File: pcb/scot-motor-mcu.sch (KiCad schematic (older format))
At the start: 49 parts, among them IC2 STM32F0xxKxTx, IC3 NCV8450A, J8 Conn_01x03_Male, P1 SWD, Q1 BC817, U1 LTV-357T, U10 74AHC1G08, U2 74HC00, U3 LTV-357T, U4 LTV-357T, U5 DRV8872DDA, Y1 Crystal_GND24

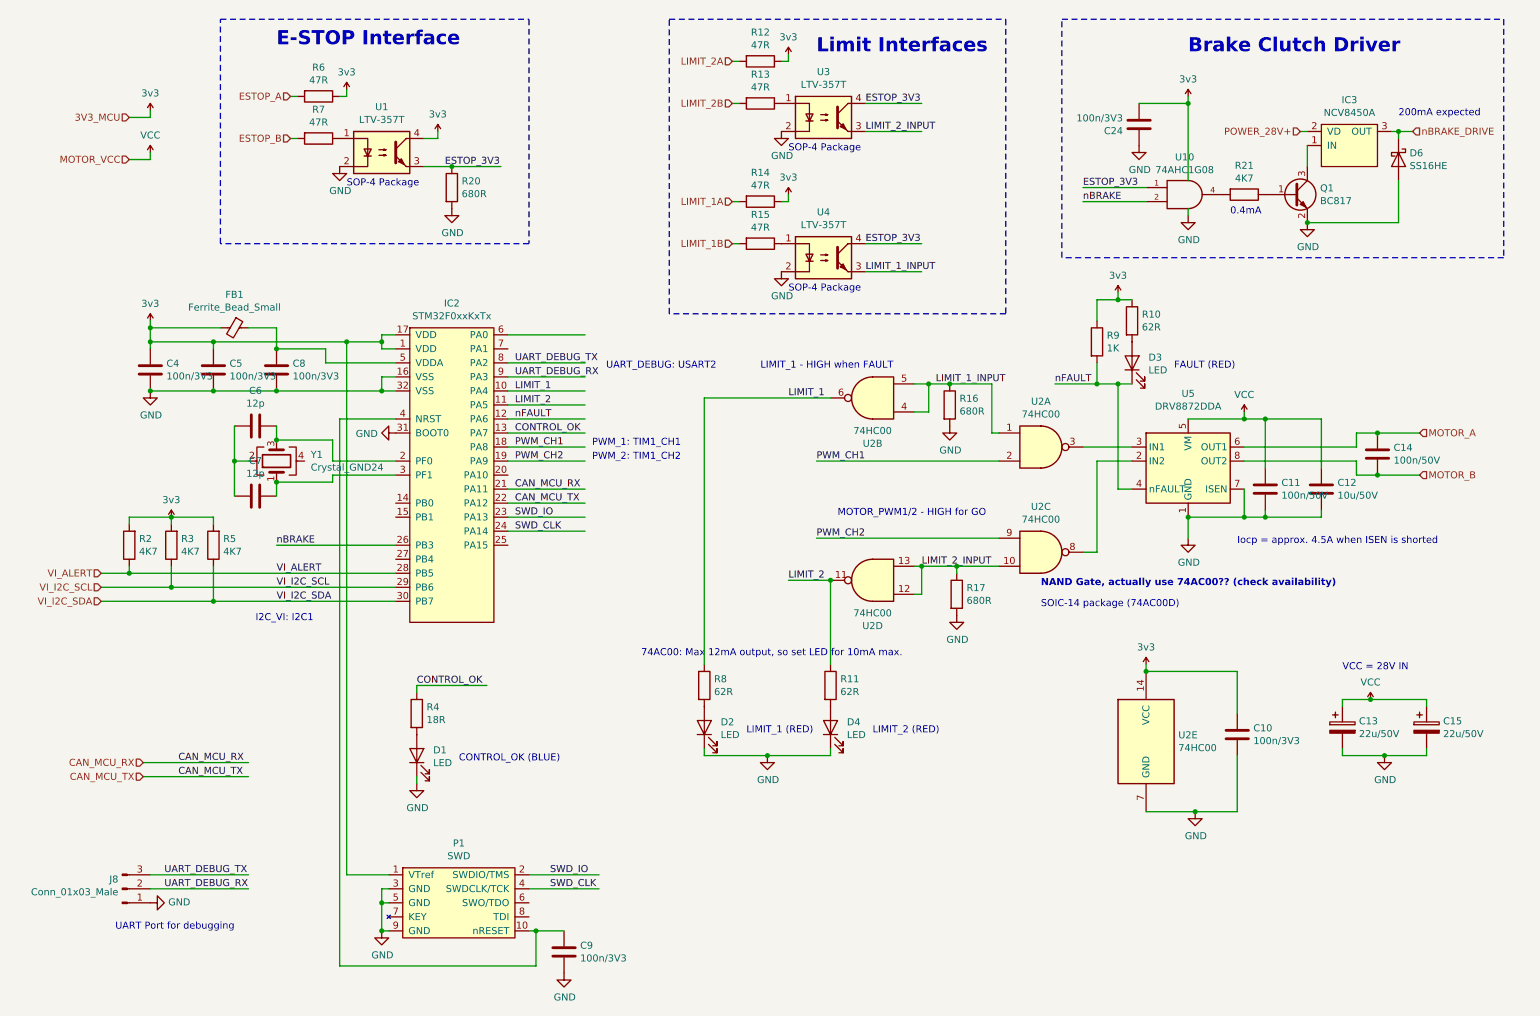
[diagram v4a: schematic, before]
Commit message: PCB progress, schematic fixes.
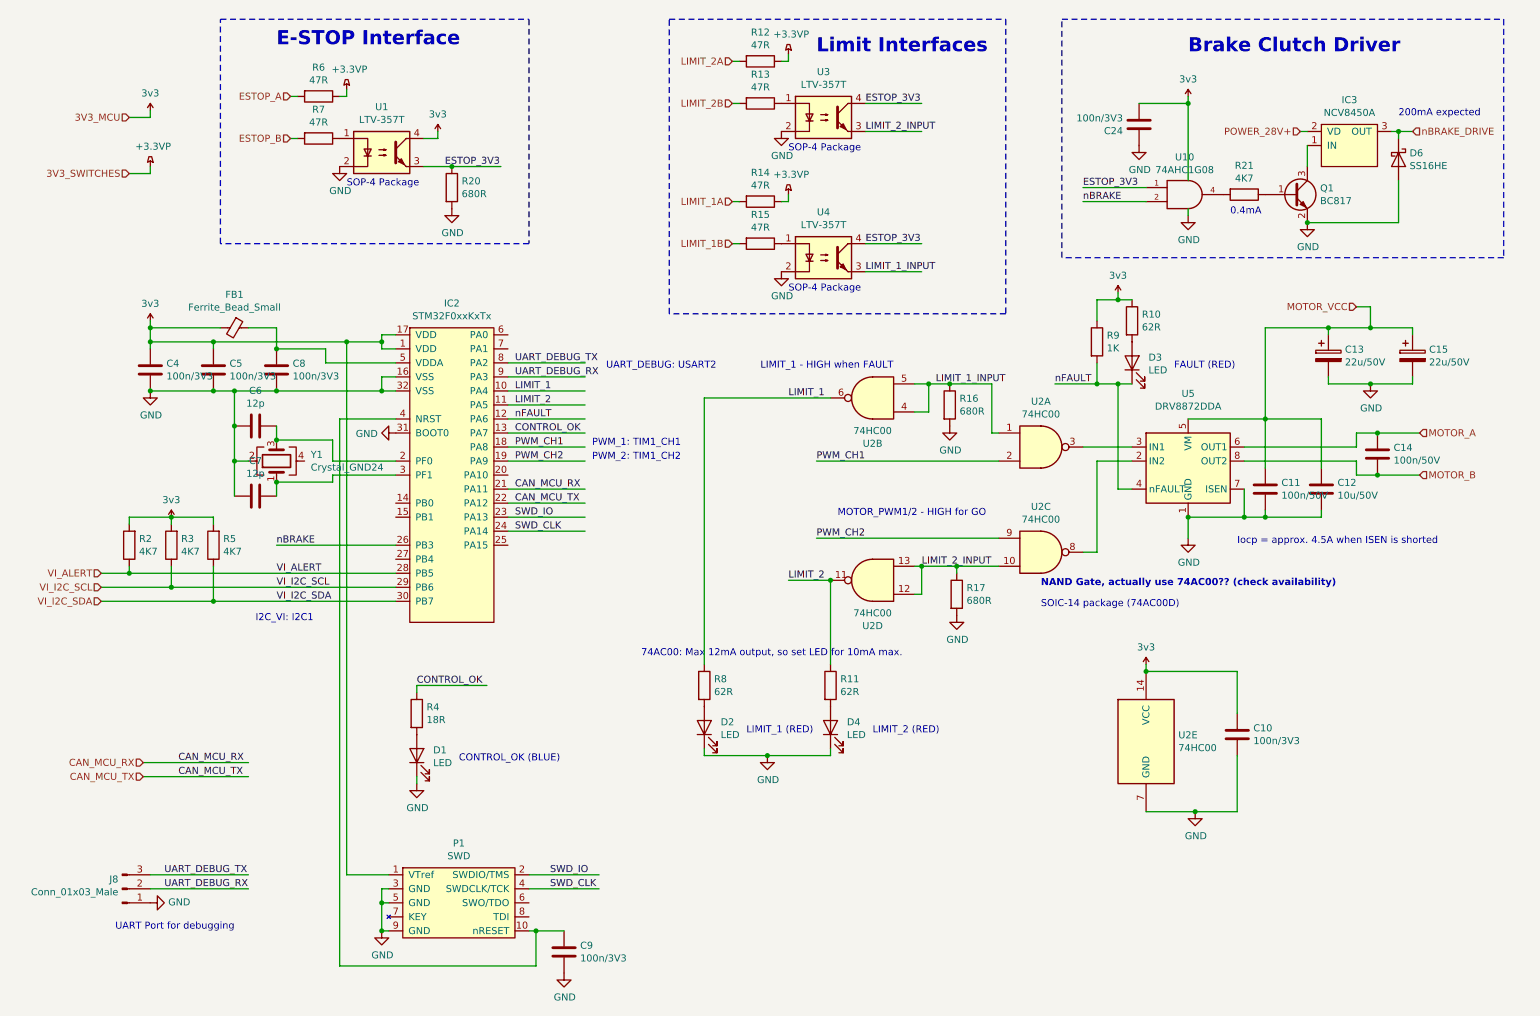
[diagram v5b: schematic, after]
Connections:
- net labels added: +3.3VP, 3V3_SWITCHES
- net labels removed: VCC
- wire segments 193 -> 196
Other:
- note removed: "VCC = 28V IN"
- moved on the sheet: C13, C15
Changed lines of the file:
@@
 	9450 3850 9450 3500
-Wire Wire Line
-	9450 3500 9300 3500
 Wire Wire Line
 	9450 3500 9850 3500
@@
 	9250 5300 8600 5300
 Connection ~ 8600 5300
-$Comp
-L agg-kicad:VCC #PWR0105
-U 1 1 5E6313B5
-P 9300 3450
-F 0 "#PWR0105" H 9300 3560 50  0001 L CNN
-F 1 "VCC" H 9300 3573 50  0000 C CNN
-F 2 "" H 9300 3450 50  0001 C CNN
-F 3 "" H 9300 3450 50  0001 C CNN
-	1    9300 3450
-	1    0    0    -1
-$EndComp
-Connection ~ 9300 3500
-Wire Wire Line
-	9300 3500 8900 3500
 Text HLabel 5650 950  0    50   Input ~ 0
 LIMIT_2A
@@
 Text Notes 6400 4200 0    50   ~ 0
 MOTOR_PWM1/2 - HIGH for GO
-Wire Wire Line
-	9300 3450 9300 3500
-$Comp
-L agg-kicad:VCC #PWR0106
-U 1 1 5E6A00FE
-P 10200 5500
-F 0 "#PWR0106" H 10200 5610 50  0001 L CNN
-F 1 "VCC" H 10200 5623 50  0000 C CNN
-F 2 "" H 10200 5500 50  0001 C CNN
-F 3 "" H 10200 5500 50  0001 C CNN
-	1    10200 5500
-	1    0    0    -1
-$EndComp
 $Comp
 L Device:CP C13
 U 1 1 5E6A417D
-P 10000 5700
-F 0 "C13" H 10118 5746 50  0000 L CNN
-F 1 "22u/50V" H 10118 5655 50  0000 L CNN
-F 2 "Capacitor_SMD:CP_Elec_8x10.5" H 10038 5550 50  0001 C CNN
-F 3 "~" H 10000 5700 50  0001 C CNN
-	1    10000 5700
+P 9900 3050
+F 0 "C13" H 10018 3096 50  0000 L CNN
+F 1 "22u/50V" H 10018 3005 50  0000 L CNN
+F 2 "Capacitor_SMD:CP_Elec_8x10.5" H 9938 2900 50  0001 C CNN
+F 3 "~" H 9900 3050 50  0001 C CNN
+	1    9900 3050
 	1    0    0    -1
 $EndComp
@@
 L Device:CP C15
 U 1 1 5E6A4BEF
-P 10600 5700
-F 0 "C15" H 10718 5746 50  0000 L CNN
-F 1 "22u/50V" H 10718 5655 50  0000 L CNN
-F 2 "Capacitor_SMD:CP_Elec_8x10.5" H 10638 5550 50  0001 C CNN
-F 3 "~" H 10600 5700 50  0001 C CNN
-	1    10600 5700
+P 10500 3050
+F 0 "C15" H 10618 3096 50  0000 L CNN
+F 1 "22u/50V" H 10618 3005 50  0000 L CNN
+F 2 "Capacitor_SMD:CP_Elec_8x10.5" H 10538 2900 50  0001 C CNN
+F 3 "~" H 10500 3050 50  0001 C CNN
+	1    10500 3050
 	1    0    0    -1
 $EndComp
 Text Notes 7850 4700 0    50   ~ 10
 NAND Gate, actually use 74AC00?? (check availability)
-Text Notes 10000 5300 0    50   ~ 0
-VCC = 28V IN
 $Comp
 L agg-kicad:STM32F0xxKxTx IC2
@@
 Text HLabel 2500 1200 0    50   Input ~ 0
 ESTOP_A
-$Comp
-L agg-kicad:3v3 #PWR0107
-U 1 1 5E8B86A8
-P 3550 1450
-F 0 "#PWR0107" H 3550 1560 50  0001 L CNN
-F 1 "3v3" H 3550 1573 50  0000 C CNN
-F 2 "" H 3550 1450 50  0001 C CNN
-F 3 "" H 3550 1450 50  0001 C CNN
-	1    3550 1450
-	1    0    0    -1
-$EndComp
 Wire Wire Line
 	8250 3800 8250 4450
@@
 Connection ~ 2400 3300
 Wire Wire Line
-	2400 3300 1950 3300
+	2400 3300 2100 3300
 Wire Wire Line
 	3250 3200 3150 3200
@@
 UART Port for debugging
 Wire Wire Line
-	10600 5900 10600 5850
-Wire Wire Line
-	10000 5900 10000 5850
-Wire Wire Line
-	10000 5550 10000 5500
-Wire Wire Line
-	10000 5500 10200 5500
-Wire Wire Line
-	10600 5550 10600 5500
-Wire Wire Line
-	10600 5500 10200 5500
-Connection ~ 10200 5500
+	10500 3250 10500 3200
+Wire Wire Line
+	9900 3250 9900 3200
+Wire Wire Line
+	9900 2900 9900 2850
+Wire Wire Line
+	10500 2900 10500 2850
 Wire Wire Line
 	6350 4650 6050 4650
@@
 $EndComp
 Wire Wire Line
-	10000 5900 10300 5900
+	9900 3250 10200 3250
 $Comp
 L power:GND #PWR0115
@@
 L power:GND #PWR0117
 U 1 1 5EB441CE
-P 10300 5900
-F 0 "#PWR0117" H 10300 5650 50  0001 C CNN
-F 1 "GND" H 10305 5727 50  0000 C CNN
-F 2 "" H 10300 5900 50  0001 C CNN
-F 3 "" H 10300 5900 50  0001 C CNN
-	1    10300 5900
-	1    0    0    -1
-$EndComp
-Connection ~ 10300 5900
-Wire Wire Line
-	10300 5900 10600 5900
+P 10200 3250
+F 0 "#PWR0117" H 10200 3000 50  0001 C CNN
+F 1 "GND" H 10205 3077 50  0000 C CNN
+F 2 "" H 10200 3250 50  0001 C CNN
+F 3 "" H 10200 3250 50  0001 C CNN
+	1    10200 3250
+	1    0    0    -1
+$EndComp
+Connection ~ 10200 3250
+Wire Wire Line
+	10200 3250 10500 3250
 Wire Wire Line
 	4050 4000 4600 4000
@@
 	1    0    0    -1
 $EndComp
-$Comp
-L agg-kicad:3v3 #PWR0119
-U 1 1 5EDDA568
-P 6050 900
-F 0 "#PWR0119" H 6050 1010 50  0001 L CNN
-F 1 "3v3" H 6050 1023 50  0000 C CNN
-F 2 "" H 6050 900 50  0001 C CNN
-F 3 "" H 6050 900 50  0001 C CNN
-	1    6050 900
-	1    0    0    -1
-$EndComp
 Wire Wire Line
 	6050 900  6050 950
@@
 L agg-kicad:3v3 #PWR0120
 U 1 1 5EF1DE63
-P 2900 1150
-F 0 "#PWR0120" H 2900 1260 50  0001 L CNN
-F 1 "3v3" H 2900 1273 50  0000 C CNN
-F 2 "" H 2900 1150 50  0001 C CNN
-F 3 "" H 2900 1150 50  0001 C CNN
-	1    2900 1150
+P 3550 1450
+F 0 "#PWR0120" H 3550 1560 50  0001 L CNN
+F 1 "3v3" H 3550 1573 50  0000 C CNN
+F 2 "" H 3550 1450 50  0001 C CNN
+F 3 "" H 3550 1450 50  0001 C CNN
+	1    3550 1450
 	1    0    0    -1
 $EndComp
@@
 	1    5850 2250
 	0    1    1    0
-$EndComp
-$Comp
-L agg-kicad:3v3 #PWR0121
-U 1 1 5EFDF057
-P 6050 1900
-F 0 "#PWR0121" H 6050 2010 50  0001 L CNN
-F 1 "3v3" H 6050 2023 50  0000 C CNN
-F 2 "" H 6050 1900 50  0001 C CNN
-F 3 "" H 6050 1900 50  0001 C CNN
-	1    6050 1900
-	1    0    0    -1
 $EndComp
 Wire Wire Line
@@
 	1950 4200 1950 4250
 Connection ~ 1650 4200
-$Comp
-L agg-kicad:VCC #PWR0124
-U 1 1 5F22A876
-P 1500 1600
-F 0 "#PWR0124" H 1500 1710 50  0001 L CNN
-F 1 "VCC" H 1500 1723 50  0000 C CNN
-F 2 "" H 1500 1600 50  0001 C CNN
-F 3 "" H 1500 1600 50  0001 C CNN
-	1    1500 1600
-	1    0    0    -1
-$EndComp
-Text HLabel 1350 1650 0    50   Input ~ 0
+Text HLabel 10100 2700 0    50   Input ~ 0
 MOTOR_VCC
-Wire Wire Line
-	1500 1600 1500 1650
-Wire Wire Line
-	1500 1650 1350 1650
 Text Notes 2250 4950 0    50   ~ 0
 I2C_VI: I2C1
@@
 Text Notes 9200 2050 0    50   ~ 0
 0.4mA
-Wire Wire Line
-	4050 2900 4600 2900
 Wire Wire Line
 	3250 4400 2400 4400
@@
 	7950 3250 8250 3250
 Connection ~ 8250 3250
+$Comp
+L power:+3.3VP #PWR0121
+U 1 1 5E945EEF
+P 1500 1700
+F 0 "#PWR0121" H 1650 1650 50  0001 C CNN
+F 1 "+3.3VP" H 1520 1843 50  0000 C CNN
+F 2 "" H 1500 1700 50  0001 C CNN
+F 3 "" H 1500 1700 50  0001 C CNN
+	1    1500 1700
+	1    0    0    -1
+$EndComp
+Text HLabel 1350 1750 0    50   Input ~ 0
+3V3_SWITCHES
+Wire Wire Line
+	1350 1750 1500 1750
+Wire Wire Line
+	1500 1750 1500 1700
+$Comp
+L power:+3.3VP #PWR0145
+U 1 1 5E962B75
+P 2900 1150
+F 0 "#PWR0145" H 3050 1100 50  0001 C CNN
+F 1 "+3.3VP" H 2920 1293 50  0000 C CNN
+F 2 "" H 2900 1150 50  0001 C CNN
+F 3 "" H 2900 1150 50  0001 C CNN
+	1    2900 1150
+	1    0    0    -1
+$EndComp
+$Comp
+L power:+3.3VP #PWR0146
+U 1 1 5E96A66C
+P 6050 900
+F 0 "#PWR0146" H 6200 850 50  0001 C CNN
+F 1 "+3.3VP" H 6070 1043 50  0000 C CNN
+F 2 "" H 6050 900 50  0001 C CNN
+F 3 "" H 6050 900 50  0001 C CNN
+	1    6050 900
+	1    0    0    -1
+$EndComp
+$Comp
+L power:+3.3VP #PWR0147
+U 1 1 5E96ADCE
+P 6050 1900
+F 0 "#PWR0147" H 6200 1850 50  0001 C CNN
+F 1 "+3.3VP" H 6070 2043 50  0000 C CNN
+F 2 "" H 6050 1900 50  0001 C CNN
+F 3 "" H 6050 1900 50  0001 C CNN
+	1    6050 1900
+	1    0    0    -1
+$EndComp
+Wire Wire Line
+	2100 3550 2100 3300
+Connection ~ 2100 3550
+Connection ~ 2100 3300
+Wire Wire Line
+	2100 3300 1950 3300
+Wire Wire Line
+	8900 3500 9450 3500
+Wire Wire Line
+	9900 2850 10200 2850
+Wire Wire Line
+	9450 3500 9450 2850
+Wire Wire Line
+	9450 2850 9900 2850
+Connection ~ 9900 2850
+Wire Wire Line
+	10200 2700 10200 2850
+Wire Wire Line
+	10100 2700 10200 2700
+Connection ~ 10200 2850
+Wire Wire Line
+	10200 2850 10500 2850
 $EndSCHEMATC

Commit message: PCB progress.
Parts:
- R21: value 4K7 -> 1K
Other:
- note removed: "0.4mA"
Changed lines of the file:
@@
 Wire Wire Line
 	9750 1550 9750 1700
-Text Notes 9200 2050 0    50   ~ 0
-0.4mA
 Wire Wire Line
 	3250 4400 2400 4400
@@
 P 9300 1900
 F 0 "R21" V 9093 1900 50  0000 C CNN
-F 1 "4K7" V 9184 1900 50  0000 C CNN
+F 1 "1K" V 9184 1900 50  0000 C CNN
 F 2 "Resistor_SMD:R_0603_1608Metric_Pad1.05x0.95mm_HandSolder" V 9230 1900 50  0001 C CNN
 F 3 "~" H 9300 1900 50  0001 C CNN

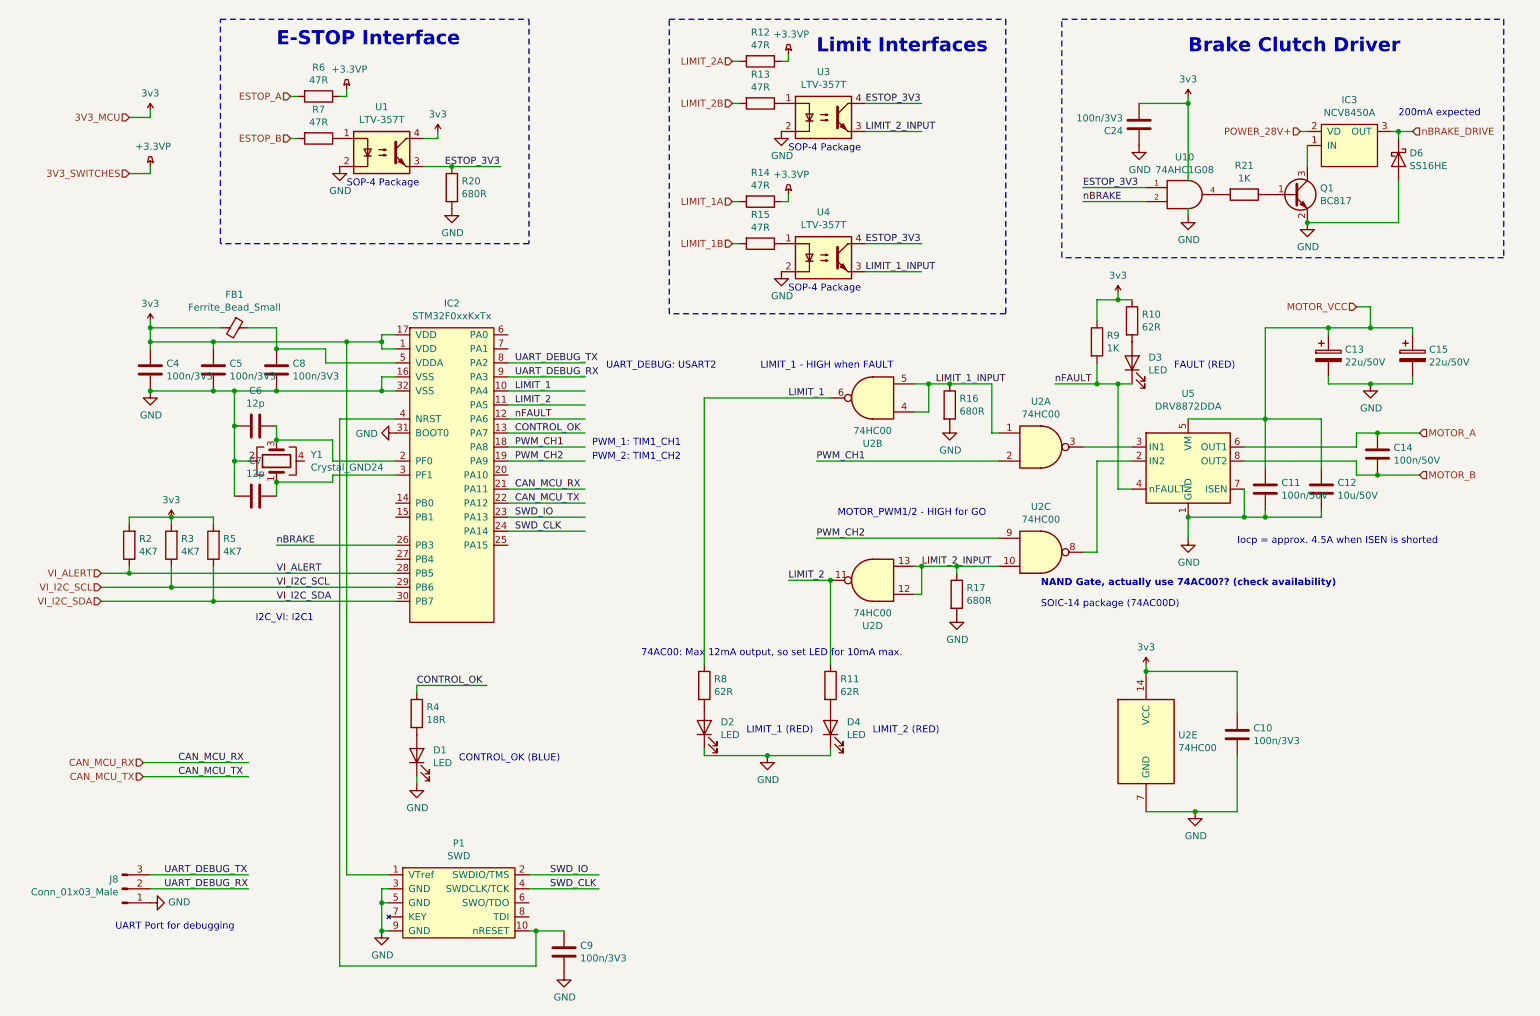
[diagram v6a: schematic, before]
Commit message: pcb: Add Clutch Release indicator.
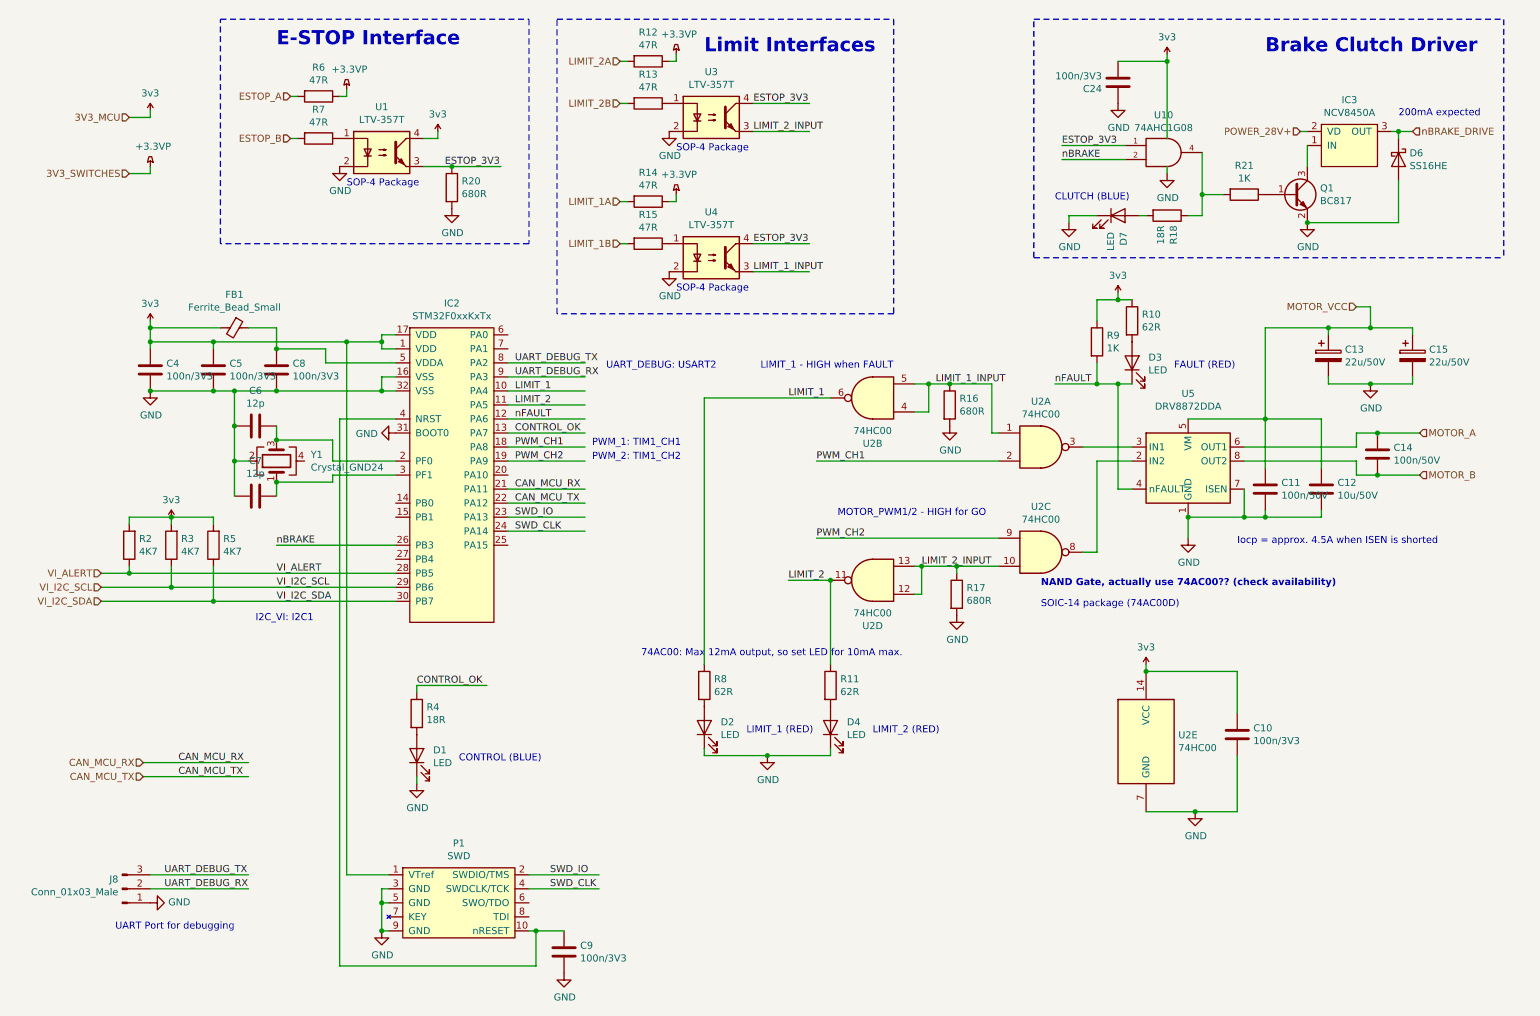
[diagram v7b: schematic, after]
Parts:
- added D7: LED, LED_SMD:LED_1210_3225Metric_Pad1.42x2.65mm_HandSolder, symbol Device:LED
- added R18: 18R, Resistor_SMD:R_0805_2012Metric_Pad1.15x1.40mm_HandSolder, symbol Device:R
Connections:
- wire segments 196 -> 203
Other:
- note added: "CLUTCH (BLUE)"
- note added: "CONTROL (BLUE)"
- note removed: "CONTROL_OK (BLUE)"
- moved on the sheet: C24, R12, R13, R14, R15, U10, U3, U4
